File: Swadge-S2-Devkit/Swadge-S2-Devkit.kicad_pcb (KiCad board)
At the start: 2 copper layers, 99.9 x 69.6 mm, 2 parts, among them U1 ESP32-S3-WROOM-1, U2 BUS_PCIexpress

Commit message: Added more to schematic
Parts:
- added BT1: Battery, Swadge_Parts:2460, B.Cu at (180.3, 101.6)
- added BT2: Battery, Swadge_Parts:2460, B.Cu at (124.5, 101.6)
- added C1: 1μF, Swadge_Parts:C_0603_1608Metric, F.Cu at (226.1, 86.4)
- added C10: 0.22μF, Swadge_Parts:C_0603_1608Metric, F.Cu at (238.6, 134.4)
- added C11: 0.01μF, Swadge_Parts:C_0603_1608Metric, F.Cu at (222.6, 139.0)
- added C12: 0.01μF, Swadge_Parts:C_0603_1608Metric, F.Cu at (236.2, 58.4)
- added C13: 0.1μF, Swadge_Parts:C_0603_1608Metric, F.Cu at (232.2, 58.4)
- added C14: 2.2μF, Swadge_Parts:C_0603_1608Metric, F.Cu at (245.8, 47.4)
- added C15: 33μF, Swadge_Parts:C_0603_1608Metric, F.Cu at (245.8, 44.9)
- added C16: 10μF, Swadge_Parts:C_0603_1608Metric, F.Cu at (224.2, 69.0)
- added C2: 22μF, Swadge_Parts:C_0603_1608Metric, F.Cu at (230.1, 83.8)
- added C3: 0.1μF, Swadge_Parts:C_0603_1608Metric, F.Cu at (214.0, 83.8)
- added C4: 1μF, Swadge_Parts:C_0603_1608Metric, F.Cu at (230.1, 86.4)
- added C5: 1μF, Swadge_Parts:C_0603_1608Metric, F.Cu at (214.0, 86.4)
- added C6: 1μF, Swadge_Parts:C_0603_1608Metric, F.Cu at (226.1, 83.8)
- added C7: 1μF, Swadge_Parts:C_0603_1608Metric, F.Cu at (277.8, 98.2)
- added C8: 22μF, Swadge_Parts:C_0603_1608Metric, F.Cu at (226.6, 136.9)
- added C9: 0.22μF, Swadge_Parts:C_0603_1608Metric, F.Cu at (218.6, 139.0)
- added D1: WS2812B, Swadge_Parts:LED_WS2812B_PLCC4_5.0x5.0mm_P3.2mm, F.Cu at (270.4, 62.7)
- added D2: WS2812B, Swadge_Parts:LED_WS2812B_PLCC4_5.0x5.0mm_P3.2mm, F.Cu at (237.9, 85.3)
- added D3: WS2812B, Swadge_Parts:LED_WS2812B_PLCC4_5.0x5.0mm_P3.2mm, F.Cu at (262.5, 62.7)
- added D4: WS2812B, Swadge_Parts:LED_WS2812B_PLCC4_5.0x5.0mm_P3.2mm, F.Cu at (245.9, 85.5)
- added D5: WS2812B, Swadge_Parts:LED_WS2812B_PLCC4_5.0x5.0mm_P3.2mm, F.Cu at (263.7, 69.2)
- added D6: WS2812B, Swadge_Parts:LED_WS2812B_PLCC4_5.0x5.0mm_P3.2mm, F.Cu at (275.3, 55.1)
- added J1: USB_B_Micro, Swadge_Parts:USB_Micro-B_Molex_47346-0001, B.Cu at (152.4, 54.3)
- added L1: 10μH, Swadge_Parts:L_0603_1608Metric, F.Cu at (212.1, 69.0)
- added LS1: Speaker, Swadge_Parts:Buzzer_12x9.5RM7.6, F.Cu at (190.5, 63.5)
- added MK1: Microphone, Swadge_Parts:CMA-4544PF-W, F.Cu at (270.3, 102.4)
- added R1: 10kΩ, Swadge_Parts:R_0603_1608Metric, F.Cu at (218.0, 83.8)
- added R10: 100, Swadge_Parts:R_0603_1608Metric, F.Cu at (232.2, 60.9)
- added R11: 47Ω, Swadge_Parts:R_0603_1608Metric, F.Cu at (216.1, 69.0)
- added R12: 47Ω, Swadge_Parts:R_0603_1608Metric, F.Cu at (220.1, 69.0)
- added R13: 1Ω, Swadge_Parts:R_0603_1608Metric, F.Cu at (208.1, 69.0)
- added R2: 10kΩ, Swadge_Parts:R_0603_1608Metric, F.Cu at (222.1, 86.4)
- added R3: 10kΩ, Swadge_Parts:R_0603_1608Metric, F.Cu at (222.1, 83.8)
- added R4: 10kΩ, Swadge_Parts:R_0603_1608Metric, F.Cu at (218.0, 86.4)
- added R5: 47kΩ, Swadge_Parts:R_0603_1608Metric, F.Cu at (230.6, 136.9)
- added R6: 10kΩ, Swadge_Parts:R_0603_1608Metric, F.Cu at (234.6, 134.4)
- added R7: 10kΩ, Swadge_Parts:R_0603_1608Metric, F.Cu at (230.6, 134.4)
- added R8: 10kΩ, Swadge_Parts:R_0603_1608Metric, F.Cu at (234.6, 136.9)
- added R9: 220kΩ, Swadge_Parts:R_0603_1608Metric, F.Cu at (223.4, 134.4)
- added SW1: 4-1437565-2, Swadge_Parts:SW_4-1437565-2, F.Cu at (180.3, 95.1)
- added SW10: 4-1437565-2, Swadge_Parts:SW_4-1437565-2, F.Cu at (112.8, 80.5)
- added SW11: 4-1437565-2, Swadge_Parts:SW_4-1437565-2, F.Cu at (148.3, 127.8)
- added SW12: 4-1437565-2, Swadge_Parts:SW_4-1437565-2, F.Cu at (156.3, 127.8)
- added SW13: touch-ring-6, Swadge_Parts:touch_six, F.Cu at (180.3, 101.6)
- added SW14: SW_SPDT, Swadge_Parts:SW_SPDT_PCM12, F.Cu at (211.6, 136.1)
- added SW2: 4-1437565-2, Swadge_Parts:SW_4-1437565-2, F.Cu at (186.9, 101.6)
- added SW3: 4-1437565-2, Swadge_Parts:SW_4-1437565-2, F.Cu at (180.3, 108.1)
- added SW4: 4-1437565-2, Swadge_Parts:SW_4-1437565-2, F.Cu at (173.8, 101.6)
- added SW5: 4-1437565-2, Swadge_Parts:SW_4-1437565-2, F.Cu at (192.0, 80.5)
- added SW6: 4-1437565-2, Swadge_Parts:SW_4-1437565-2, F.Cu at (124.5, 95.1)
- added SW7: 4-1437565-2, Swadge_Parts:SW_4-1437565-2, F.Cu at (131.0, 101.6)
- added SW8: 4-1437565-2, Swadge_Parts:SW_4-1437565-2, F.Cu at (124.5, 108.1)
- added SW9: 4-1437565-2, Swadge_Parts:SW_4-1437565-2, F.Cu at (117.9, 101.6)
- added U3: AP1117-33, Swadge_Parts:SOT-223-3_TabPin2, F.Cu at (269.8, 111.9)
- added U4: GS321-TR, Swadge_Parts:SOT-23-5, F.Cu at (219.0, 135.4)
- added U5: QMA7981, Swadge_Parts:QMA6981, F.Cu at (249.9, 45.8)
- added U6: INGHAi_GSPK2308P-8R0.5W, Swadge_Parts:INGHAi GSPK2308P-8R0.5W, F.Cu at (114.3, 63.5)
- U2: moved to F.Cu
- moved U2 184.8 mm to (142.9, 147.8), turned to 0 degrees
- moved U1 183.2 mm to (152.4, 101.6)
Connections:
- U1 pad 1: unconnected-(U1-Pad1) -> GND
- U1 pad 10: unconnected-(U1-Pad10) -> SDA
- U1 pad 11: unconnected-(U1-Pad11) -> SCL
- U1 pad 12: unconnected-(U1-Pad12) -> MIC
- U1 pad 13: unconnected-(U1-Pad13) -> USB_D-
- U1 pad 14: unconnected-(U1-Pad14) -> USB_D+
- U1 pad 15: unconnected-(U1-Pad15) -> TFT_LEDA
- U1 pad 16: unconnected-(U1-Pad16) -> TFT_RESET
- U1 pad 17: unconnected-(U1-Pad17) -> TOUCH_1
- U1 pad 18: unconnected-(U1-Pad18) -> TOUCH_2
- U1 pad 19: unconnected-(U1-Pad19) -> TOUCH_3
- U1 pad 2: unconnected-(U1-Pad2) -> +3V3
- U1 pad 20: unconnected-(U1-Pad20) -> TOUCH_4
- U1 pad 21: unconnected-(U1-Pad21) -> TOUCH_5
- U1 pad 22: unconnected-(U1-Pad22) -> TOUCH_6
- U1 pad 23: unconnected-(U1-Pad23) -> TFT_RS
- U1 pad 24: unconnected-(U1-Pad24) -> TFT_SCL
- U1 pad 25: unconnected-(U1-Pad25) -> TFT_SDA
- U1 pad 26: unconnected-(U1-Pad26) -> TFT_CS
- U1 pad 27: unconnected-(U1-Pad27) -> BTN_11
- U1 pad 28: unconnected-(U1-Pad28) -> BTN_12
- U1 pad 29: unconnected-(U1-Pad29) -> BTN_8
- U1 pad 3: unconnected-(U1-Pad3) -> Net-(C1-Pad1)
- U1 pad 30: unconnected-(U1-Pad30) -> BTN_9
- U1 pad 31: unconnected-(U1-Pad31) -> BTN_10
- U1 pad 32: unconnected-(U1-Pad32) -> LED
- U1 pad 34: unconnected-(U1-Pad34) -> BZR
- U1 pad 35: unconnected-(U1-Pad35) -> SPK
- U1 pad 36: unconnected-(U1-Pad36) -> RX
- U1 pad 37: unconnected-(U1-Pad37) -> TX
- U1 pad 38: unconnected-(U1-Pad38) -> BTN_7
- U1 pad 39: unconnected-(U1-Pad39) -> BTN_6
- U1 pad 4: unconnected-(U1-Pad4) -> BTN_1
- U1 pad 40: unconnected-(U1-Pad40) -> GND
- U1 pad 41: unconnected-(U1-Pad41) -> GND
- U1 pad 5: unconnected-(U1-Pad5) -> BTN_2
- U1 pad 6: unconnected-(U1-Pad6) -> BTN_3
- U1 pad 7: unconnected-(U1-Pad7) -> BTN_4
- U1 pad 8: unconnected-(U1-Pad8) -> BTN_5
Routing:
- added copper zone on B.Cu, net GND
- added copper zone on F.Cu, net GND
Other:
- board size 99.9 x 69.6 mm -> 99.9 x 99.9 mm

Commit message: Added TFT, vib motor
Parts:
- added C17: 10μF, Swadge_Parts:C_0603_1608Metric, F.Cu at (78.7, 96.5)
- added D7: D, Swadge_Parts:D_SMA, F.Cu at (213.4, 48.3)
- added M1: Motor_DC, Swadge_Parts:Z30C1B839982L, F.Cu at (210.8, 40.6)
- added Q1: Q_NPN_BEC, Swadge_Parts:SOT-23, F.Cu at (225.7, 40.6)
- added Q2: Q_NPN_BEC, Swadge_Parts:SOT-23, F.Cu at (43.2, 91.4)
- added R14: 330Ω, Swadge_Parts:R_0603_1608Metric, F.Cu at (219.4, 47.2)
- added R15: 22Ω, Swadge_Parts:R_0603_1608Metric, F.Cu at (40.6, 101.6)
- added R16: 10kΩ, Swadge_Parts:R_0603_1608Metric, F.Cu at (43.0, 95.0)
- added R17: 1kΩ, Swadge_Parts:R_0603_1608Metric, F.Cu at (36.6, 101.6)
- added U7: TFT-1.14, Swadge_Parts:TFT-1.14, F.Cu at (62.4, 111.0)
- LS1: value Speaker -> Buzzer
- R10: value 100 -> 100Ω
- moved D6 117.9 mm to (157.4, 56.3), turned to 150 degrees
- moved D5 117.0 mm to (147.4, 56.3), turned to -150 degrees
- moved D3 115.6 mm to (147.4, 73.7), turned to -30 degrees
- moved D1 108.0 mm to (162.4, 65.0), turned to 90 degrees
- moved D4 105.5 mm to (142.4, 65.0), turned to -90 degrees
- moved D2 81.4 mm to (157.4, 73.7), turned to 30 degrees
- moved R3 55.7 mm to (167.6, 71.9), turned to -90 degrees
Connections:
- U1 pad 9: unconnected-(U1-Pad9) -> MOTOR
- U2 pad A1: unconnected-(U2-PadA1) -> GND
- U2 pad A11: unconnected-(U2-PadA11) -> LED_OUT
- U2 pad A12: unconnected-(U2-PadA12) -> MIC
- U2 pad A15: unconnected-(U2-PadA15) -> TX
- U2 pad A16: unconnected-(U2-PadA16) -> RX
- U2 pad A18: unconnected-(U2-PadA18) -> +5V
- U2 pad A2: unconnected-(U2-PadA2) -> SCL
- U2 pad A3: unconnected-(U2-PadA3) -> SDA
- U2 pad A4: unconnected-(U2-PadA4) -> _RES
- U2 pad A8: unconnected-(U2-PadA8) -> +3V3
- U2 pad B1: unconnected-(U2-PadB1) -> GND
- U2 pad B11: unconnected-(U2-PadB11) -> LED_OUT
- U2 pad B12: unconnected-(U2-PadB12) -> MIC
- U2 pad B15: unconnected-(U2-PadB15) -> TX
- U2 pad B16: unconnected-(U2-PadB16) -> RX
- U2 pad B18: unconnected-(U2-PadB18) -> +5V
- U2 pad B2: unconnected-(U2-PadB2) -> SCL
- U2 pad B3: unconnected-(U2-PadB3) -> SDA
- U2 pad B4: unconnected-(U2-PadB4) -> _RES
- U2 pad B8: unconnected-(U2-PadB8) -> +3V3
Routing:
- net Net-(D2-Pad2): track 0.00 -> 6.90 mm
- net Net-(D5-Pad2): track 0.00 -> 6.90 mm
- net Net-(D4-Pad2): track 0.00 -> 6.77 mm
- net Net-(D1-Pad2): track 0.00 -> 6.77 mm
- net Net-(D3-Pad2): track 0.00 -> 6.57 mm

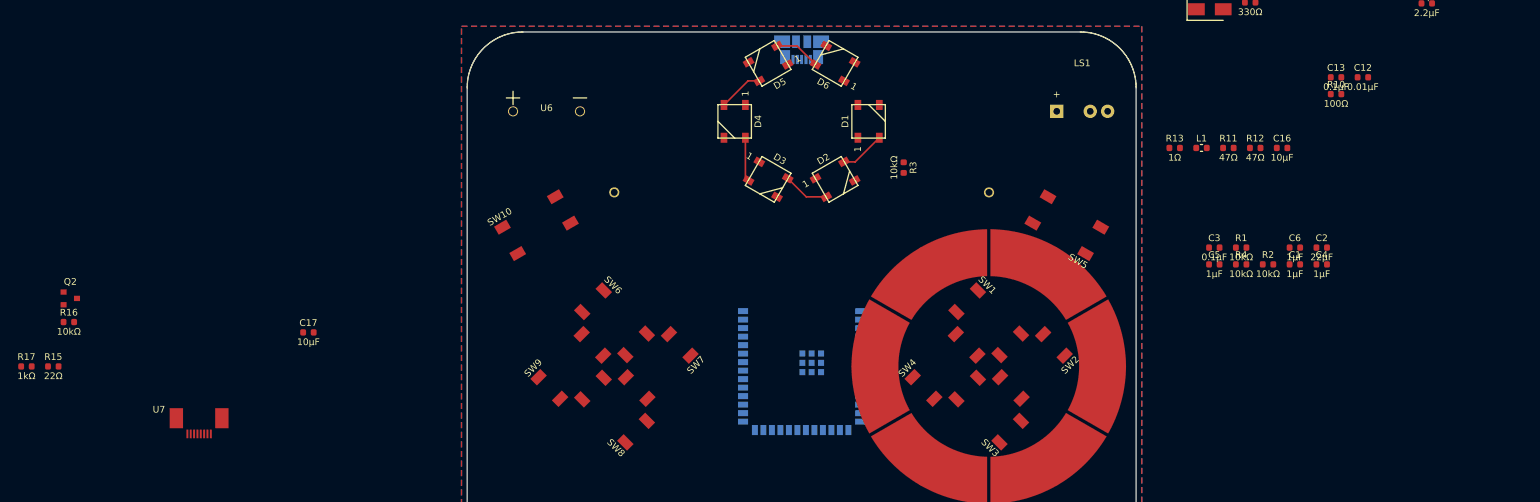
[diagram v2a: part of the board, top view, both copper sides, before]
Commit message: Updated layout
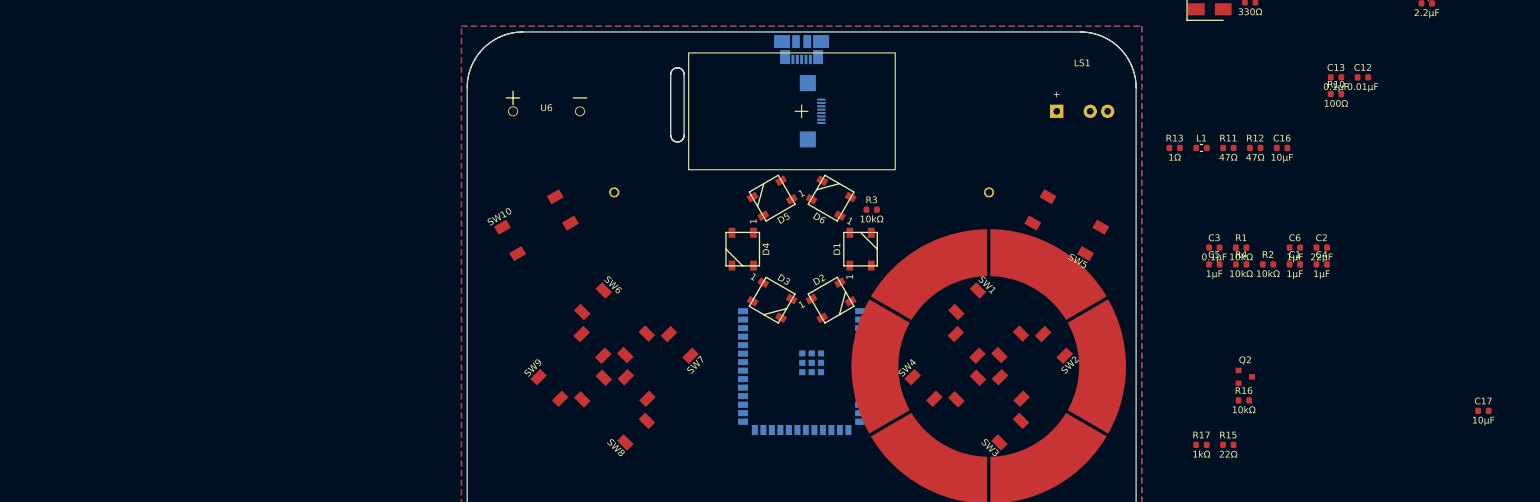
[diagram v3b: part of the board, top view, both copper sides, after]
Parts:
- Ue: renamed from U7; moved to B.Cu
- moved C17 175.9 mm to (254.2, 108.2)
- moved R15 175.9 mm to (216.1, 113.3)
- moved R17 175.9 mm to (212.1, 113.3)
- moved Q2 175.9 mm to (218.7, 103.2)
- moved R16 175.9 mm to (218.4, 106.7)
- moved Ue 103.8 mm to (154.7, 63.5), turned to -90 degrees
- moved D6 20.1 mm to (156.8, 76.5)
- moved D5 20.1 mm to (148.0, 76.5)
- moved D1 19.1 mm to (161.2, 84.1)
- moved D4 19.1 mm to (143.6, 84.1)
- moved D2 18.1 mm to (156.8, 91.7)
- moved D3 18.1 mm to (148.0, 91.7)
- moved R3 7.89 mm to (162.9, 78.2), turned to 0 degrees
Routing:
- net Net-(D2-Pad2): track 6.90 -> 0.00 mm
- net Net-(D5-Pad2): track 6.90 -> 0.00 mm
- net Net-(D4-Pad2): track 6.77 -> 0.00 mm
- net Net-(D1-Pad2): track 6.77 -> 0.00 mm
- net Net-(D3-Pad2): track 6.57 -> 0.00 mm
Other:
- rule pad_to_mask_clearance: 0.2 -> 0

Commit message: Updated PCB
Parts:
- C1, C17, C2, C3, Q2, R1, R15, R16, R17, R2, R4: moved to B.Cu
- moved C14 189.5 mm to (86.0, 149.3)
- moved U5 188.4 mm to (90.3, 145.9)
- moved C12 168.3 mm to (94.7, 149.5)
- moved C13 168.3 mm to (90.7, 149.5)
- moved R11 153.4 mm to (82.8, 144.8)
- moved R12 153.4 mm to (86.8, 144.8)
- moved C15 150.9 mm to (95.4, 57.8)
- moved MK1 141.4 mm to (133.4, 137.6)
- moved C1 140.6 mm to (86.4, 102.5), turned to 180 degrees
- moved C2 134.6 mm to (96.1, 97.2), turned to 180 degrees
- moved R1 132.3 mm to (86.5, 97.5), turned to 180 degrees
- moved R2 130.8 mm to (92.4, 103.3), turned to 180 degrees
- moved C16 129.6 mm to (94.7, 62.8)
- moved L1 122.9 mm to (90.0, 54.8)
- moved R4 122.8 mm to (96.4, 103.3), turned to 180 degrees
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
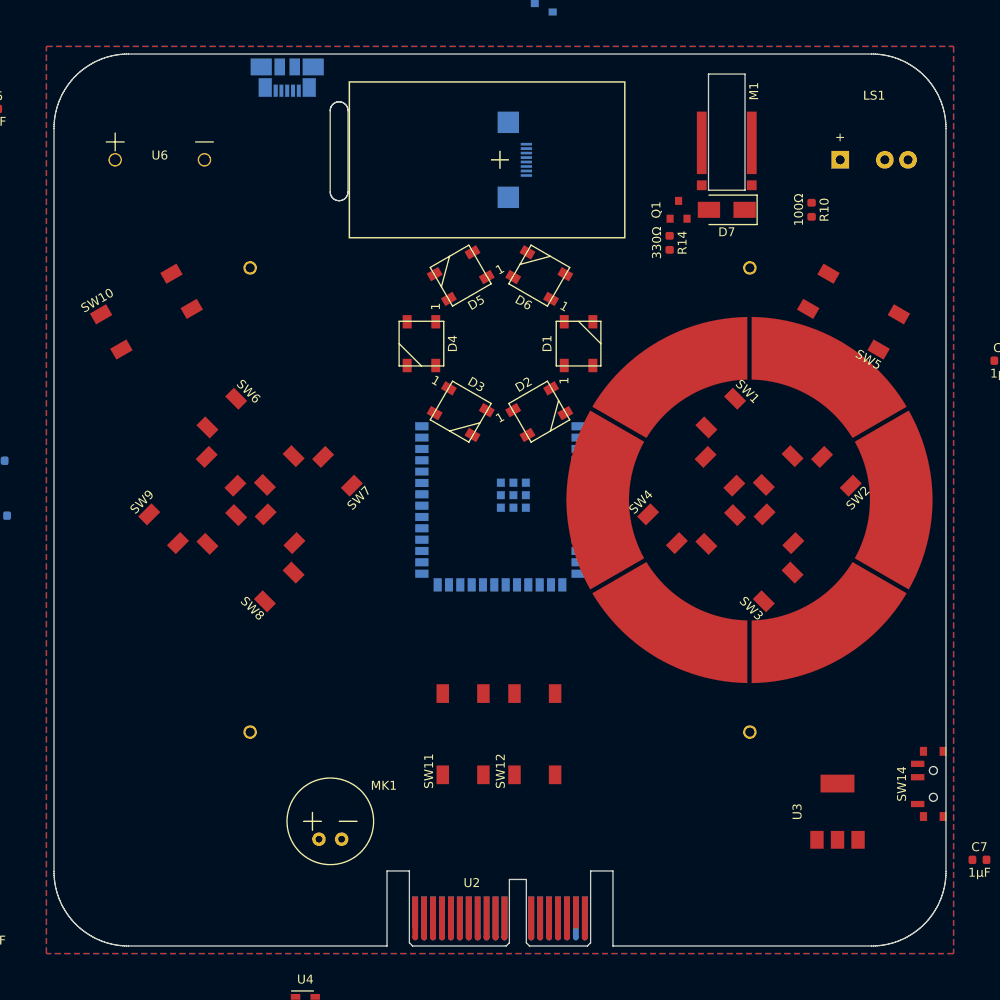
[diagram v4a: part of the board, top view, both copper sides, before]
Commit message: Connected PCIe, replaced S3 with S2, cleanup
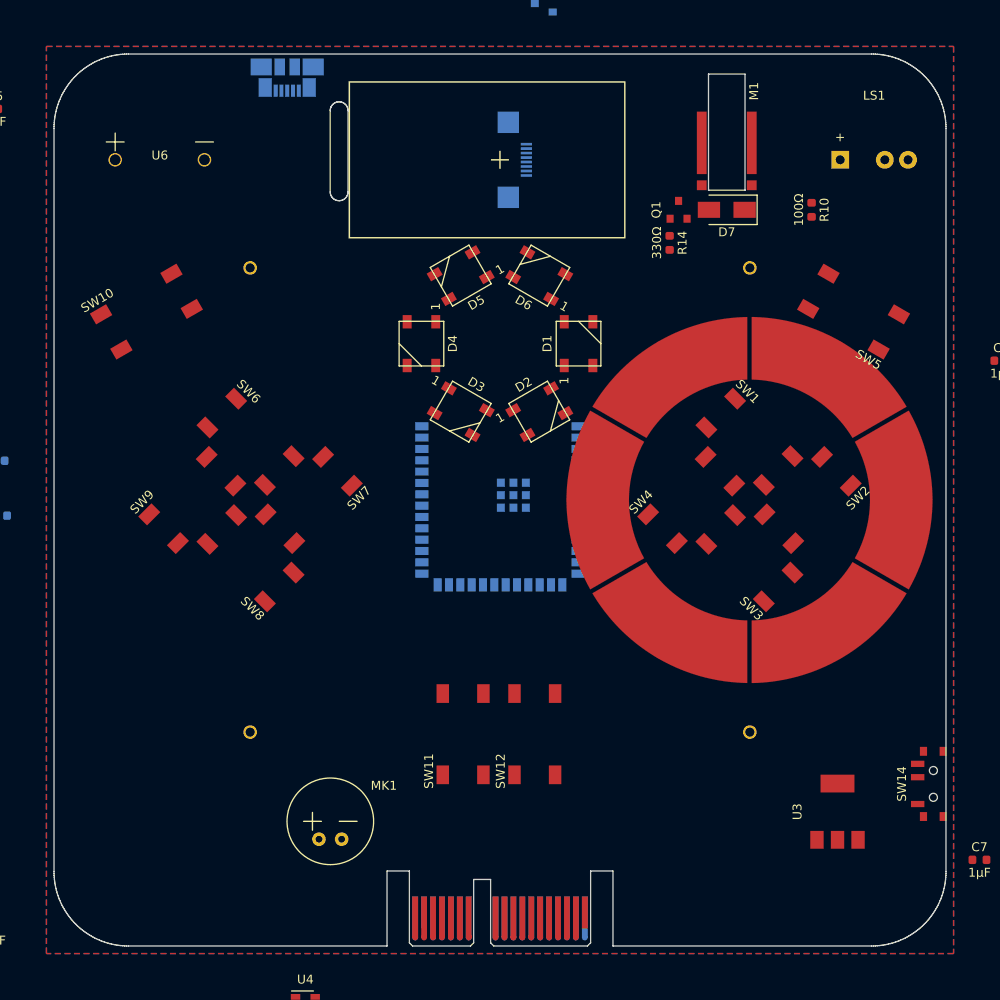
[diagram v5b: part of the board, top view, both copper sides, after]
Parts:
- removed Ue: TFT-1.14, Swadge_Parts:TFT-1.14
- added U7: TFT-1.14, Swadge_Parts:TFT-1.14, B.Cu at (154.7, 63.5)
- added U8: TFT_DISPLAY, Swadge_Parts:NULL, F.Cu at (132.9, 91.7)
- U1: value ESP32-S3-WROOM-1 -> ESP32-S2-SOLO; footprint Swadge_Parts:ESP32-S3-WROOM-1 -> Swadge_Parts:ESP32-S2-SOLO
- U2: moved to B.Cu
- moved U2 19.0 mm to (161.9, 147.8), turned to 180 degrees
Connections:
- R3 pad 1: Net-(D1-Pad4) -> +3V3
- R3 pad 2: LED -> SDA
- R4 pad 1: +3V3 -> Net-(D1-Pad4)
- R4 pad 2: SDA -> LED
- U2 pad A12: MIC -> MOTOR
- U2 pad A13: unconnected-(U2-PadA13) -> SPK
- U2 pad A14: unconnected-(U2-PadA14) -> BZR
- U2 pad A17: unconnected-(U2-PadA17) -> LED
- U2 pad A2: SCL -> BTN_11
- U2 pad A3: SDA -> TFT_RESET
- U2 pad A4: _RES -> TFT_CS
- U2 pad A5: unconnected-(U2-PadA5) -> MIC
- U2 pad A6: unconnected-(U2-PadA6) -> SCL
- U2 pad A7: unconnected-(U2-PadA7) -> SDA
- U2 pad B12: MIC -> MOTOR
- U2 pad B13: unconnected-(U2-PadB13) -> SPK
- U2 pad B14: unconnected-(U2-PadB14) -> BZR
- U2 pad B17: unconnected-(U2-PadB17) -> LED
- U2 pad B2: SCL -> BTN_11
- U2 pad B3: SDA -> TFT_RESET
- U2 pad B4: _RES -> TFT_CS
- U2 pad B5: unconnected-(U2-PadB5) -> MIC
- U2 pad B6: unconnected-(U2-PadB6) -> SCL
- U2 pad B7: unconnected-(U2-PadB7) -> SDA
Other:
- outline, holes or cut-outs redrawn
